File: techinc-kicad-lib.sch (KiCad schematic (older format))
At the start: 8 parts

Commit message: add esp-12, rotate esp-03
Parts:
- removed U?: ESP-03, ~, symbol ESP-03
- added U?: ESP-03, ~, symbol ESP-03
- added U?: ESP-12, ~, symbol ESP-12
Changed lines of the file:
@@
-$EndComp
-$Comp
-L ESP-03 U?
-U 1 1 55088450
-P 3650 4550
-F 0 "U?" H 3650 5050 60  0000 C CNN
-F 1 "ESP-03" H 3650 4050 60  0000 C CNN
-F 2 "~" H 3650 4550 60  0000 C CNN
-F 3 "~" H 3650 4550 60  0000 C CNN
-	1    3650 4550
-	1    0    0    -1
 $EndComp
 $Comp
@@
 	1    0    0    -1
 $EndComp
+$Comp
+L ESP-03 U?
+U 1 1 55089ECB
+P 3450 4600
+F 0 "U?" H 3450 5100 60  0000 C CNN
+F 1 "ESP-03" H 3450 4100 60  0000 C CNN
+F 2 "~" H 3450 4600 60  0000 C CNN
+F 3 "~" H 3450 4600 60  0000 C CNN
+	1    3450 4600
+	1    0    0    -1
+$EndComp
+$Comp
+L ESP-12 U?
+U 1 1 55089EDA
+P 5500 4600
+F 0 "U?" H 5500 5150 60  0000 C CNN
+F 1 "ESP-12" H 5500 4050 60  0000 C CNN
+F 2 "~" H 5500 4600 60  0000 C CNN
+F 3 "~" H 5500 4600 60  0000 C CNN
+	1    5500 4600
+	1    0    0    -1
+$EndComp

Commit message: add esp-07v2/08v2
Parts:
- removed IC?: MAX490, ~, symbol MAX490
- removed U?: ESP-03, ~, symbol ESP-03
- removed U?: ESP-12, ~, symbol ESP-12
- added IC2: MAX490, ~, symbol MAX490_DIP/SO
- added U2: ESP-03, ~, symbol ESP-03/07V1/08V1
- added U5: ESP-12, ~, symbol ESP-12/07V2/08V2
- added U6: ESP-07v1, ~, symbol ESP-03/07V1/08V1
- added U7: ESP-08v1, ~, symbol ESP-03/07V1/08V1
- added U8: ESP-08v2, ~, symbol ESP-12/07V2/08V2
- added U9: ESP-07v2, ~, symbol ESP-12/07V2/08V2
- D1: renamed from D?; footprint ~ -> (none)
- gave numbers to parts that had none: 5
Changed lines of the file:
@@
 $EndDescr
 $Comp
-L WS2812 U?
+L WS2812 U3
 U 1 1 55084C1F
 P 3700 1850
-F 0 "U?" H 3700 2250 60  0000 C CNN
+F 0 "U3" H 3700 2250 60  0000 C CNN
 F 1 "WS2812" H 3700 1500 60  0000 C CNN
 F 2 "~" H 3700 1850 60  0000 C CNN
@@
 $EndComp
 $Comp
-L WS2812B U?
+L WS2812B U4
 U 1 1 55084C2E
 P 5000 1850
-F 0 "U?" H 5000 2100 60  0000 C CNN
+F 0 "U4" H 5000 2100 60  0000 C CNN
 F 1 "WS2812B" H 5000 1600 60  0000 C CNN
 F 2 "~" H 5000 1850 60  0000 C CNN
@@
 $EndComp
 $Comp
-L MAX490 IC?
-U 1 1 55084CA0
-P 1850 3300
-F 0 "IC?" H 1850 3800 60  0000 C CNN
-F 1 "MAX490" H 1850 2800 60  0000 C CNN
-F 2 "~" H 1850 3300 60  0000 C CNN
-F 3 "~" H 1850 3300 60  0000 C CNN
-	1    1850 3300
-	1    0    0    -1
-$EndComp
-$Comp
-L SAMSUNG_RGB_LED_5050_SPMFCT5606N0S0A1E0 D?
+L SAMSUNG_RGB_LED_5050_SPMFCT5606N0S0A1E0 D1
 U 1 1 55084CAF
 P 3700 3350
-F 0 "D?" H 3700 3000 60  0000 C CNN
+F 0 "D1" H 3700 3000 60  0000 C CNN
 F 1 "SAMSUNG_RGB_LED_5050_SPMFCT5606N0S0A1E0" H 3800 3650 60  0000 C CNN
-F 2 "~" H 3800 2350 60  0000 C CNN
-F 3 "~" H 3800 2350 60  0000 C CNN
+F 2 "" H 3800 2350 60  0000 C CNN
+F 3 "" H 3800 2350 60  0000 C CNN
 	1    3700 3350
 	1    0    0    -1
 $EndComp
 $Comp
-L WS2801 IC?
+L WS2801 IC1
 U 1 1 55085816
 P 1550 1800
-F 0 "IC?" H 1550 2300 60  0000 C CNN
+F 0 "IC1" H 1550 2300 60  0000 C CNN
 F 1 "WS2801" H 1550 1300 60  0000 C CNN
 F 2 "~" H 1550 1800 60  0000 C CNN
@@
 $EndComp
 $Comp
-L WS2811 IC?
+L WS2811 IC3
 U 1 1 55086D92
 P 2600 1850
-F 0 "IC?" H 2600 2200 60  0000 C CNN
+F 0 "IC3" H 2600 2200 60  0000 C CNN
 F 1 "WS2811" H 2600 1500 60  0000 C CNN
 F 2 "~" H 2600 1850 60  0000 C CNN
@@
 $EndComp
 $Comp
-L ESP-01 U?
+L ESP-01 U1
 U 1 1 5508885F
 P 1800 4550
-F 0 "U?" H 1800 4900 60  0000 C CNN
+F 0 "U1" H 1800 4900 60  0000 C CNN
 F 1 "ESP-01" H 1800 4200 60  0000 C CNN
 F 2 "~" H 1800 4550 60  0000 C CNN
@@
 $EndComp
 $Comp
-L ESP-03 U?
-U 1 1 55089ECB
-P 3450 4600
-F 0 "U?" H 3450 5100 60  0000 C CNN
-F 1 "ESP-03" H 3450 4100 60  0000 C CNN
-F 2 "~" H 3450 4600 60  0000 C CNN
-F 3 "~" H 3450 4600 60  0000 C CNN
-	1    3450 4600
+L ESP-12/07V2/08V2 U5
+U 1 1 5508AE6C
+P 5500 4650
+F 0 "U5" H 5500 5200 60  0000 C CNN
+F 1 "ESP-12" H 5500 4100 60  0000 C CNN
+F 2 "~" H 5500 4650 60  0000 C CNN
+F 3 "~" H 5500 4650 60  0000 C CNN
+	1    5500 4650
 	1    0    0    -1
 $EndComp
 $Comp
-L ESP-12 U?
-U 1 1 55089EDA
-P 5500 4600
-F 0 "U?" H 5500 5150 60  0000 C CNN
-F 1 "ESP-12" H 5500 4050 60  0000 C CNN
-F 2 "~" H 5500 4600 60  0000 C CNN
-F 3 "~" H 5500 4600 60  0000 C CNN
-	1    5500 4600
+L ESP-12/07V2/08V2 U9
+U 1 1 5508AE79
+P 8100 4650
+F 0 "U9" H 8100 5200 60  0000 C CNN
+F 1 "ESP-07v2" H 8100 4100 60  0000 C CNN
+F 2 "~" H 8100 4650 60  0000 C CNN
+F 3 "~" H 8100 4650 60  0000 C CNN
+	1    8100 4650
 	1    0    0    -1
 $EndComp
+$Comp
+L ESP-12/07V2/08V2 U8
+U 1 1 5508AE7F
+P 7350 5900
+F 0 "U8" H 7350 6450 60  0000 C CNN
+F 1 "ESP-08v2" H 7350 5350 60  0000 C CNN
+F 2 "~" H 7350 5900 60  0000 C CNN
+F 3 "~" H 7350 5900 60  0000 C CNN
+	1    7350 5900
+	1    0    0    -1
+$EndComp
+$Comp
+L MAX490_DIP/SO IC2
+U 1 1 5508B567
+P 1750 3300
+F 0 "IC2" H 1750 3800 60  0000 C CNN
+F 1 "MAX490" H 1750 2800 60  0000 C CNN
+F 2 "~" H 1750 3300 60  0000 C CNN
+F 3 "~" H 1750 3300 60  0000 C CNN
+	1    1750 3300
+	1    0    0    -1
+$EndComp
+$Comp
+L ESP-03/07V1/08V1 U2
+U 1 1 5508BA93
+P 1850 6050
+F 0 "U2" H 1850 6550 60  0000 C CNN
+F 1 "ESP-03" H 1850 5550 60  0000 C CNN
+F 2 "~" H 1850 6050 60  0000 C CNN
+F 3 "~" H 1850 6050 60  0000 C CNN
+	1    1850 6050
+	1    0    0    -1
+$EndComp
+$Comp
+L ESP-03/07V1/08V1 U6
+U 1 1 5508BAA0
+P 3400 6050
+F 0 "U6" H 3400 6550 60  0000 C CNN
+F 1 "ESP-07v1" H 3400 5550 60  0000 C CNN
+F 2 "~" H 3400 6050 60  0000 C CNN
+F 3 "~" H 3400 6050 60  0000 C CNN
+	1    3400 6050
+	1    0    0    -1
+$EndComp
+$Comp
+L ESP-03/07V1/08V1 U7
+U 1 1 5508BAA6
+P 5050 6100
+F 0 "U7" H 5050 6600 60  0000 C CNN
+F 1 "ESP-08v1" H 5050 5600 60  0000 C CNN
+F 2 "~" H 5050 6100 60  0000 C CNN
+F 3 "~" H 5050 6100 60  0000 C CNN
+	1    5050 6100
+	1    0    0    -1
+$EndComp

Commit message: add arduino shield modules
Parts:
- added U10, U11, U12: ARDUINOSHIELD, ~, symbol ARDUINOSHIELD
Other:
- moved on the sheet: D1, IC1, IC2, IC3, U1, U3, U4
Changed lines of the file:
@@
 LIBS:samsung_rgb_led_5050_spmfct5606n0s0a1e0
 LIBS:esp8266
+LIBS:arduino
 LIBS:techinc-kicad-lib-cache
 EELAYER 27 0
@@
 Sheet 1 1
 Title ""
-Date "17 mar 2015"
+Date "21 mar 2015"
 Rev ""
 Comp ""
@@
 L WS2812 U3
 U 1 1 55084C1F
-P 3700 1850
-F 0 "U3" H 3700 2250 60  0000 C CNN
-F 1 "WS2812" H 3700 1500 60  0000 C CNN
-F 2 "~" H 3700 1850 60  0000 C CNN
-F 3 "~" H 3700 1850 60  0000 C CNN
-	1    3700 1850
+P 2900 1000
+F 0 "U3" H 2900 1400 60  0000 C CNN
+F 1 "WS2812" H 2900 650 60  0000 C CNN
+F 2 "~" H 2900 1000 60  0000 C CNN
+F 3 "~" H 2900 1000 60  0000 C CNN
+	1    2900 1000
 	1    0    0    -1
 $EndComp
@@
 L WS2812B U4
 U 1 1 55084C2E
-P 5000 1850
-F 0 "U4" H 5000 2100 60  0000 C CNN
-F 1 "WS2812B" H 5000 1600 60  0000 C CNN
-F 2 "~" H 5000 1850 60  0000 C CNN
-F 3 "~" H 5000 1850 60  0000 C CNN
-	1    5000 1850
+P 4100 1000
+F 0 "U4" H 4100 1250 60  0000 C CNN
+F 1 "WS2812B" H 4100 750 60  0000 C CNN
+F 2 "~" H 4100 1000 60  0000 C CNN
+F 3 "~" H 4100 1000 60  0000 C CNN
+	1    4100 1000
 	1    0    0    -1
 $EndComp
@@
 L SAMSUNG_RGB_LED_5050_SPMFCT5606N0S0A1E0 D1
 U 1 1 55084CAF
-P 3700 3350
-F 0 "D1" H 3700 3000 60  0000 C CNN
-F 1 "SAMSUNG_RGB_LED_5050_SPMFCT5606N0S0A1E0" H 3800 3650 60  0000 C CNN
-F 2 "" H 3800 2350 60  0000 C CNN
-F 3 "" H 3800 2350 60  0000 C CNN
-	1    3700 3350
+P 2650 2200
+F 0 "D1" H 2650 1850 60  0000 C CNN
+F 1 "SAMSUNG_RGB_LED_5050_SPMFCT5606N0S0A1E0" H 2750 2500 60  0000 C CNN
+F 2 "" H 2750 1200 60  0000 C CNN
+F 3 "" H 2750 1200 60  0000 C CNN
+	1    2650 2200
 	1    0    0    -1
 $EndComp
@@
 L WS2801 IC1
 U 1 1 55085816
-P 1550 1800
-F 0 "IC1" H 1550 2300 60  0000 C CNN
-F 1 "WS2801" H 1550 1300 60  0000 C CNN
-F 2 "~" H 1550 1800 60  0000 C CNN
-F 3 "~" H 1550 1800 60  0000 C CNN
-	1    1550 1800
+P 1100 1000
+F 0 "IC1" H 1100 1500 60  0000 C CNN
+F 1 "WS2801" H 1100 500 60  0000 C CNN
+F 2 "~" H 1100 1000 60  0000 C CNN
+F 3 "~" H 1100 1000 60  0000 C CNN
+	1    1100 1000
 	1    0    0    -1
 $EndComp
@@
 L WS2811 IC3
 U 1 1 55086D92
-P 2600 1850
-F 0 "IC3" H 2600 2200 60  0000 C CNN
-F 1 "WS2811" H 2600 1500 60  0000 C CNN
-F 2 "~" H 2600 1850 60  0000 C CNN
-F 3 "~" H 2600 1850 60  0000 C CNN
-	1    2600 1850
+P 1950 1000
+F 0 "IC3" H 1950 1350 60  0000 C CNN
+F 1 "WS2811" H 1950 650 60  0000 C CNN
+F 2 "~" H 1950 1000 60  0000 C CNN
+F 3 "~" H 1950 1000 60  0000 C CNN
+	1    1950 1000
 	1    0    0    -1
 $EndComp
@@
 L ESP-01 U1
 U 1 1 5508885F
-P 1800 4550
-F 0 "U1" H 1800 4900 60  0000 C CNN
-F 1 "ESP-01" H 1800 4200 60  0000 C CNN
-F 2 "~" H 1800 4550 60  0000 C CNN
-F 3 "~" H 1800 4550 60  0000 C CNN
-	1    1800 4550
+P 5500 4400
+F 0 "U1" H 5500 4750 60  0000 C CNN
+F 1 "ESP-01" H 5500 4050 60  0000 C CNN
+F 2 "~" H 5500 4400 60  0000 C CNN
+F 3 "~" H 5500 4400 60  0000 C CNN
+	1    5500 4400
 	1    0    0    -1
 $EndComp
@@
 L ESP-12/07V2/08V2 U5
 U 1 1 5508AE6C
-P 5500 4650
-F 0 "U5" H 5500 5200 60  0000 C CNN
-F 1 "ESP-12" H 5500 4100 60  0000 C CNN
-F 2 "~" H 5500 4650 60  0000 C CNN
-F 3 "~" H 5500 4650 60  0000 C CNN
-	1    5500 4650
+P 4650 3250
+F 0 "U5" H 4650 3800 60  0000 C CNN
+F 1 "ESP-12" H 4650 2700 60  0000 C CNN
+F 2 "~" H 4650 3250 60  0000 C CNN
+F 3 "~" H 4650 3250 60  0000 C CNN
+	1    4650 3250
 	1    0    0    -1
 $EndComp
@@
 L ESP-12/07V2/08V2 U9
 U 1 1 5508AE79
-P 8100 4650
-F 0 "U9" H 8100 5200 60  0000 C CNN
-F 1 "ESP-07v2" H 8100 4100 60  0000 C CNN
-F 2 "~" H 8100 4650 60  0000 C CNN
-F 3 "~" H 8100 4650 60  0000 C CNN
-	1    8100 4650
+P 7250 3250
+F 0 "U9" H 7250 3800 60  0000 C CNN
+F 1 "ESP-07v2" H 7250 2700 60  0000 C CNN
+F 2 "~" H 7250 3250 60  0000 C CNN
+F 3 "~" H 7250 3250 60  0000 C CNN
+	1    7250 3250
 	1    0    0    -1
 $EndComp
@@
 L ESP-12/07V2/08V2 U8
 U 1 1 5508AE7F
-P 7350 5900
-F 0 "U8" H 7350 6450 60  0000 C CNN
-F 1 "ESP-08v2" H 7350 5350 60  0000 C CNN
-F 2 "~" H 7350 5900 60  0000 C CNN
-F 3 "~" H 7350 5900 60  0000 C CNN
-	1    7350 5900
+P 9850 3250
+F 0 "U8" H 9850 3800 60  0000 C CNN
+F 1 "ESP-08v2" H 9850 2700 60  0000 C CNN
+F 2 "~" H 9850 3250 60  0000 C CNN
+F 3 "~" H 9850 3250 60  0000 C CNN
+	1    9850 3250
 	1    0    0    -1
 $EndComp
@@
 L MAX490_DIP/SO IC2
 U 1 1 5508B567
-P 1750 3300
-F 0 "IC2" H 1750 3800 60  0000 C CNN
-F 1 "MAX490" H 1750 2800 60  0000 C CNN
-F 2 "~" H 1750 3300 60  0000 C CNN
-F 3 "~" H 1750 3300 60  0000 C CNN
-	1    1750 3300
+P 1150 2200
+F 0 "IC2" H 1150 2700 60  0000 C CNN
+F 1 "MAX490" H 1150 1700 60  0000 C CNN
+F 2 "~" H 1150 2200 60  0000 C CNN
+F 3 "~" H 1150 2200 60  0000 C CNN
+	1    1150 2200
 	1    0    0    -1
 $EndComp
@@
 L ESP-03/07V1/08V1 U2
 U 1 1 5508BA93
-P 1850 6050
-F 0 "U2" H 1850 6550 60  0000 C CNN
-F 1 "ESP-03" H 1850 5550 60  0000 C CNN
-F 2 "~" H 1850 6050 60  0000 C CNN
-F 3 "~" H 1850 6050 60  0000 C CNN
-	1    1850 6050
+P 7050 4400
+F 0 "U2" H 7050 4900 60  0000 C CNN
+F 1 "ESP-03" H 7050 3900 60  0000 C CNN
+F 2 "~" H 7050 4400 60  0000 C CNN
+F 3 "~" H 7050 4400 60  0000 C CNN
+	1    7050 4400
 	1    0    0    -1
 $EndComp
@@
 L ESP-03/07V1/08V1 U6
 U 1 1 5508BAA0
-P 3400 6050
-F 0 "U6" H 3400 6550 60  0000 C CNN
-F 1 "ESP-07v1" H 3400 5550 60  0000 C CNN
-F 2 "~" H 3400 6050 60  0000 C CNN
-F 3 "~" H 3400 6050 60  0000 C CNN
-	1    3400 6050
+P 8600 4400
+F 0 "U6" H 8600 4900 60  0000 C CNN
+F 1 "ESP-07v1" H 8600 3900 60  0000 C CNN
+F 2 "~" H 8600 4400 60  0000 C CNN
+F 3 "~" H 8600 4400 60  0000 C CNN
+	1    8600 4400
 	1    0    0    -1
 $EndComp
@@
 L ESP-03/07V1/08V1 U7
 U 1 1 5508BAA6
-P 5050 6100
-F 0 "U7" H 5050 6600 60  0000 C CNN
-F 1 "ESP-08v1" H 5050 5600 60  0000 C CNN
-F 2 "~" H 5050 6100 60  0000 C CNN
-F 3 "~" H 5050 6100 60  0000 C CNN
-	1    5050 6100
+P 10150 4400
+F 0 "U7" H 10150 4900 60  0000 C CNN
+F 1 "ESP-08v1" H 10150 3900 60  0000 C CNN
+F 2 "~" H 10150 4400 60  0000 C CNN
+F 3 "~" H 10150 4400 60  0000 C CNN
+	1    10150 4400
 	1    0    0    -1
 $EndComp
+$Comp
+L ARDUINOSHIELD U10
+U 1 1 550D6612
+P 5950 1600
+F 0 "U10" H 5950 2550 60  0000 C CNN
+F 1 "ARDUINOSHIELD" H 5950 600 60  0000 C CNN
+F 2 "~" H 5950 1600 60  0000 C CNN
+F 3 "~" H 5950 1600 60  0000 C CNN
+	1    5950 1600
+	1    0    0    -1
+$EndComp
+$Comp
+L ARDUINOSHIELD U11
+U 1 1 550D661F
+P 8000 1600
+F 0 "U11" H 8000 2550 60  0000 C CNN
+F 1 "ARDUINOSHIELD" H 8000 600 60  0000 C CNN
+F 2 "~" H 8000 1600 60  0000 C CNN
+F 3 "~" H 8000 1600 60  0000 C CNN
+	1    8000 1600
+	1    0    0    -1
+$EndComp
+$Comp
+L ARDUINOSHIELD U12
+U 1 1 550D6639
+P 10050 1600
+F 0 "U12" H 10050 2550 60  0000 C CNN
+F 1 "ARDUINOSHIELD" H 10050 600 60  0000 C CNN
+F 2 "~" H 10050 1600 60  0000 C CNN
+F 3 "~" H 10050 1600 60  0000 C CNN
+	1    10050 1600
+	1    0    0    -1
+$EndComp

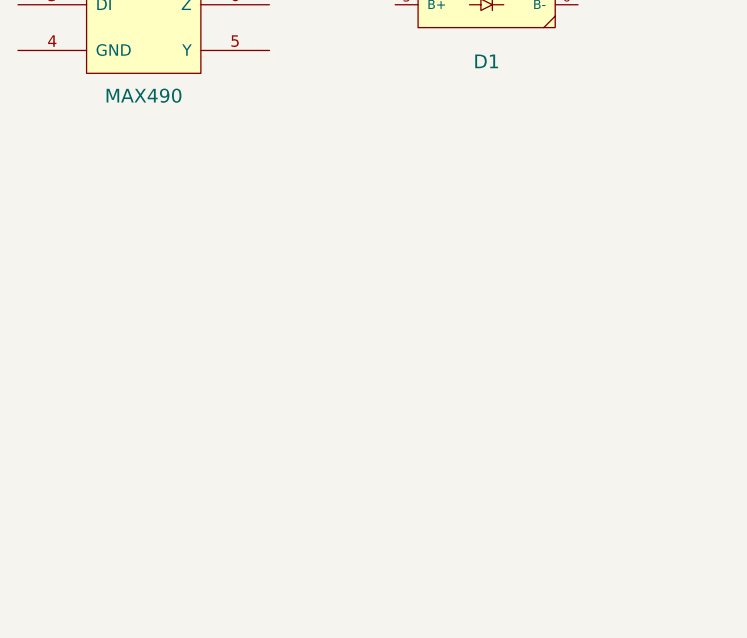
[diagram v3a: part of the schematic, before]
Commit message: add NH-14 nixie tube lib/footprint
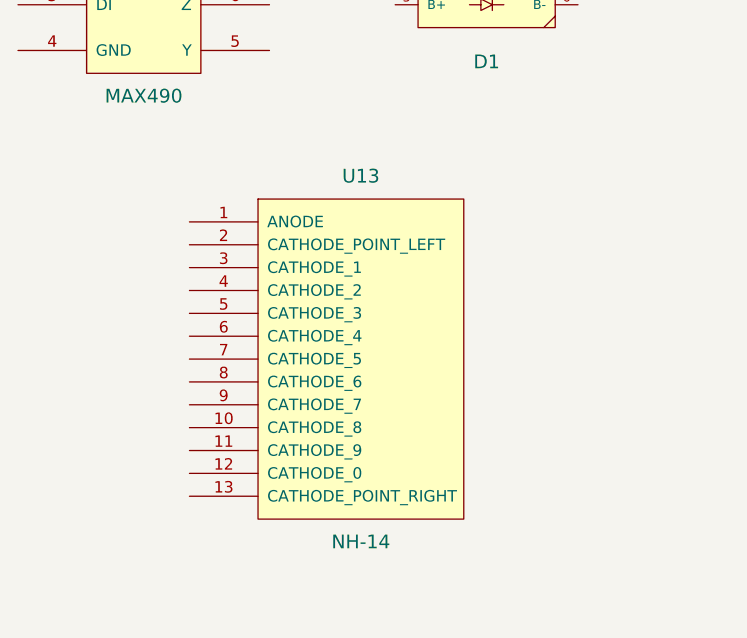
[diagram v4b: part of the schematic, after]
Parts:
- added U13: NH-14, ~, symbol NH-14
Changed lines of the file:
@@
 LIBS:esp8266
 LIBS:arduino
+LIBS:nixie
 LIBS:techinc-kicad-lib-cache
 EELAYER 27 0
@@
 Sheet 1 1
 Title ""
-Date "21 mar 2015"
+Date "28 mar 2015"
 Rev ""
 Comp ""
@@
 	1    0    0    -1
 $EndComp
+$Comp
+L NH-14 U13
+U 1 1 5516DB97
+P 2100 3850
+F 0 "U13" H 2100 4650 60  0000 C CNN
+F 1 "NH-14" H 2100 3050 60  0000 C CNN
+F 2 "~" H 1750 3900 60  0000 C CNN
+F 3 "~" H 1750 3900 60  0000 C CNN
+	1    2100 3850
+	1    0    0    -1
+$EndComp

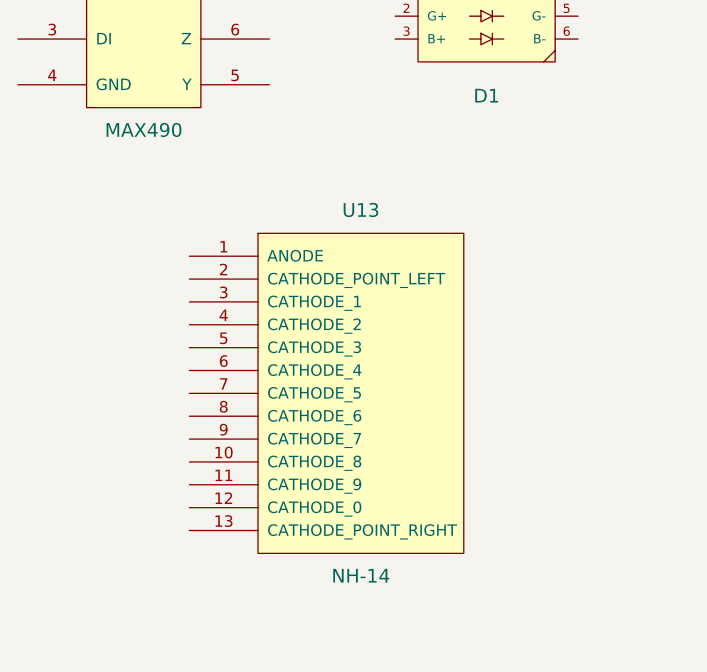
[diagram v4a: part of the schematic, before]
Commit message: rename nixie tube component/lib
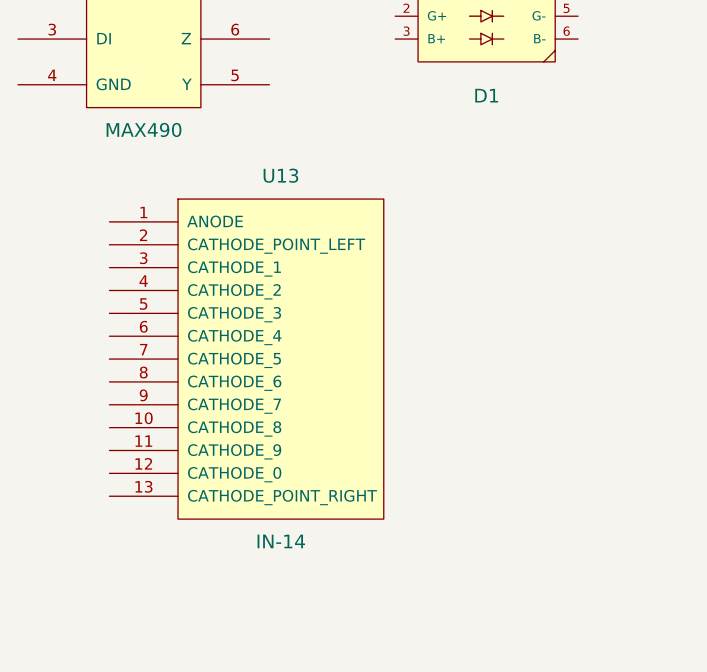
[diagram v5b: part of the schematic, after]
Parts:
- removed U13: NH-14, ~, symbol NH-14
- added U13: IN-14, ~, symbol IN-14
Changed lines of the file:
@@
 $EndComp
 $Comp
-L NH-14 U13
-U 1 1 5516DB97
-P 2100 3850
-F 0 "U13" H 2100 4650 60  0000 C CNN
-F 1 "NH-14" H 2100 3050 60  0000 C CNN
-F 2 "~" H 1750 3900 60  0000 C CNN
-F 3 "~" H 1750 3900 60  0000 C CNN
-	1    2100 3850
+L IN-14 U13
+U 1 1 5516FC18
+P 1750 3700
+F 0 "U13" H 1750 4500 60  0000 C CNN
+F 1 "IN-14" H 1750 2900 60  0000 C CNN
+F 2 "~" H 1400 3750 60  0000 C CNN
+F 3 "~" H 1400 3750 60  0000 C CNN
+	1    1750 3700
 	1    0    0    -1
 $EndComp

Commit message: fix esp pinout, add SOT voltage regulator
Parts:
- added U14: LM6206, SOT23, symbol LM6206
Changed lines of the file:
@@
 LIBS:arduino
 LIBS:nixie
+LIBS:lm6206
 LIBS:techinc-kicad-lib-cache
 EELAYER 27 0
@@
 Sheet 1 1
 Title ""
-Date "28 mar 2015"
+Date "31 mar 2015"
 Rev ""
 Comp ""
@@
 	1    0    0    -1
 $EndComp
+$Comp
+L LM6206 U14
+U 1 1 551AFB4D
+P 3050 4450
+F 0 "U14" H 2850 4250 40  0000 C CNN
+F 1 "LM6206" H 3050 4250 40  0000 L CNN
+F 2 "SOT23" H 3050 4350 30  0000 C CIN
+F 3 "~" H 3050 4450 60  0000 C CNN
+	1    3050 4450
+	1    0    0    -1
+$EndComp
